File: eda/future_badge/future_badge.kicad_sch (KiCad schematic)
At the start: 0 parts

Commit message: schematic start
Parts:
- added D? (x4): LED_WS2812D_THT_5mm, 0_local:LED_D5.0mm-4_WS2812D_front, symbol 0_local:LED_WS2812D_THT_5mm
- added D? (x14): LED_THT_5mm, 0_local:LED_D5.0mm-2, symbol 0_local:LED_THT_5mm
- added U?: ESP-12F, RF_Module:ESP-12E, symbol RF_Module:ESP-12F
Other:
- note added: "battery choice, 3aaa?"
- note added: "capacitors"
- note added: "test pins for flashing mcu"
- note added: "usb choice? yes/no/flash only"
- note added: "voltage reg transistor"

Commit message: more stuff
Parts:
- removed D? (x8): LED_THT_5mm, 0_local:LED_D5.0mm-2, symbol 0_local:LED_THT_5mm
- removed U?: ESP-12F, RF_Module:ESP-12E, symbol RF_Module:ESP-12F
- added D? (x4): LED_Two_Color_CC_THT_3mm, 0_local:LED_D3.0mm-3-TwoColor_backsilk, symbol 0_local:LED_Two_Color_CC_THT_3mm
- added U?: ESP32-WROOM-32, RF_Module:ESP32-WROOM-32, symbol 0_local:ESP32-WROOM-32
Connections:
- new net: U?.1 (GND), U?.15 (GND), U?.38 (GND), U?.39 (GND)
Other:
- note removed: "test pins for flashing mcu"
- note removed: "usb choice? yes/no/flash only"
- note removed: "voltage reg transistor"
- moved on the sheet: D?

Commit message: more test code and esp32 sch and fp and 3d
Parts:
- removed D? (x6): LED_THT_5mm, 0_local:LED_D5.0mm-2, symbol 0_local:LED_THT_5mm
- removed U?: ESP32-WROOM-32, RF_Module:ESP32-WROOM-32, symbol 0_local:ESP32-WROOM-32
- added U?: ESP32-WROOM-32-DEVKIT, 0_local:ESP32_DEVKIT_V1, symbol 0_local:ESP32-WROOM-32-DEVKIT
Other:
- note removed: "battery choice, 3aaa?"
- note removed: "capacitors"
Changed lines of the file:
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@@
     (company "Crafted by @alt_bier a.k.a. Richard Gowen")
-  )
-  (text "battery choice, 3aaa?" (at 41.91 153.67 0)
-    (effects (font (size 1.27 1.27)) (justify left bottom))
-  )
-  (text "capacitors" (at 57.15 25.4 0)
-    (effects (font (size 1.27 1.27)) (justify left bottom))
   )
   (symbol (lib_id "0_local:LED_Two_Color_CC_THT_3mm") (at 64.77 120.65 0) (unit 1)
@@
     (pin "4")
   )
-  (symbol (lib_id "0_local:LED_THT_5mm") (at 128.27 121.92 0) (unit 1)
+  (symbol (lib_id "0_local:LED_Two_Color_CC_THT_3mm") (at 60.96 95.25 0) (unit 1)
     (in_bom yes) (on_board yes) (fields_autoplaced)
-    (property "Reference" "D?" (id 0) (at 126.6698 116.9756 0))
-    (property "Value" "LED_THT_5mm" (id 1) (at 126.6698 119.5125 0))
-    (property "Footprint" "0_local:LED_D5.0mm-2" (id 2) (at 128.27 128.27 0)
+    (property "Reference" "D?" (id 0) (at 59.7535 82.6602 0))
+    (property "Value" "LED_Two_Color_CC_THT_3mm" (id 1) (at 59.7535 85.1971 0))
+    (property "Footprint" "0_local:LED_D3.0mm-3-TwoColor_backsilk" (id 2) (at 62.23 107.95 0)
       (effects (font (size 1.27 1.27)) hide)
     )
-    (property "Datasheet" "~" (id 3) (at 128.27 121.92 0)
+    (property "Datasheet" "~" (id 3) (at 59.309 95.123 0)
       (effects (font (size 1.27 1.27)) hide)
     )
     (pin "1")
     (pin "2")
+    (pin "3")
   )
-  (symbol (lib_id "0_local:LED_THT_5mm") (at 124.46 107.95 0) (unit 1)
+  (symbol (lib_id "0_local:ESP32-WROOM-32-DEVKIT") (at 205.74 62.23 0) (unit 1)
     (in_bom yes) (on_board yes) (fields_autoplaced)
-    (property "Reference" "D?" (id 0) (at 122.8598 103.0056 0))
-    (property "Value" "LED_THT_5mm" (id 1) (at 122.8598 105.5425 0))
-    (property "Footprint" "0_local:LED_D5.0mm-2" (id 2) (at 124.46 114.3 0)
+    (property "Reference" "U?" (id 0) (at 205.74 21.7002 0))
+    (property "Value" "ESP32-WROOM-32-DEVKIT" (id 1) (at 205.74 24.2371 0))
+    (property "Footprint" "0_local:ESP32_DEVKIT_V1" (id 2) (at 206.121 100.965 0)
       (effects (font (size 1.27 1.27)) hide)
     )
-    (property "Datasheet" "~" (id 3) (at 124.46 107.95 0)
-      (effects (font (size 1.27 1.27)) hide)
-    )
-    (pin "1")
-    (pin "2")
-  )
-  (symbol (lib_id "0_local:LED_THT_5mm") (at 132.08 77.47 0) (unit 1)
-    (in_bom yes) (on_board yes) (fields_autoplaced)
-    (property "Reference" "D?" (id 0) (at 130.4798 72.5256 0))
-    (property "Value" "LED_THT_5mm" (id 1) (at 130.4798 75.0625 0))
-    (property "Footprint" "0_local:LED_D5.0mm-2" (id 2) (at 132.08 83.82 0)
-      (effects (font (size 1.27 1.27)) hide)
-    )
-    (property "Datasheet" "~" (id 3) (at 132.08 77.47 0)
-      (effects (font (size 1.27 1.27)) hide)
-    )
-    (pin "1")
-    (pin "2")
-  )
-  (symbol (lib_id "0_local:ESP32-WROOM-32") (at 201.93 62.23 0) (unit 1)
-    (in_bom yes) (on_board yes) (fields_autoplaced)
-    (property "Reference" "U?" (id 0) (at 203.9494 25.5102 0)
-      (effects (font (size 1.27 1.27)) (justify left))
-    )
-    (property "Value" "ESP32-WROOM-32" (id 1) (at 203.9494 28.0471 0)
-      (effects (font (size 1.27 1.27)) (justify left))
-    )
-    (property "Footprint" "RF_Module:ESP32-WROOM-32" (id 2) (at 201.93 100.33 0)
-      (effects (font (size 1.27 1.27)) hide)
-    )
-    (property "Datasheet" "https://www.espressif.com/sites/default/files/documentation/esp32-wroom-32_datasheet_en.pdf" (id 3) (at 194.31 60.96 0)
+    (property "Datasheet" "https://www.espressif.com/sites/default/files/documentation/esp32-wroom-32_datasheet_en.pdf" (id 3) (at 206.121 104.14 0)
       (effects (font (size 1.27 1.27)) hide)
     )
@@
     (pin "3")
     (pin "30")
-    (pin "31")
-    (pin "32")
-    (pin "33")
-    (pin "34")
-    (pin "35")
-    (pin "36")
-    (pin "37")
-    (pin "38")
-    (pin "39")
     (pin "4")
     (pin "5")
@@
     (pin "8")
     (pin "9")
-  )
-  (symbol (lib_id "0_local:LED_Two_Color_CC_THT_3mm") (at 60.96 95.25 0) (unit 1)
-    (in_bom yes) (on_board yes) (fields_autoplaced)
-    (property "Reference" "D?" (id 0) (at 59.7535 82.6602 0))
-    (property "Value" "LED_Two_Color_CC_THT_3mm" (id 1) (at 59.7535 85.1971 0))
-    (property "Footprint" "0_local:LED_D3.0mm-3-TwoColor_backsilk" (id 2) (at 62.23 107.95 0)
-      (effects (font (size 1.27 1.27)) hide)
-    )
-    (property "Datasheet" "~" (id 3) (at 59.309 95.123 0)
-      (effects (font (size 1.27 1.27)) hide)
-    )
-    (pin "1")
-    (pin "2")
-    (pin "3")
-  )
-  (symbol (lib_id "0_local:LED_THT_5mm") (at 116.84 77.47 0) (unit 1)
-    (in_bom yes) (on_board yes) (fields_autoplaced)
-    (property "Reference" "D?" (id 0) (at 115.2398 72.5256 0))
-    (property "Value" "LED_THT_5mm" (id 1) (at 115.2398 75.0625 0))
-    (property "Footprint" "0_local:LED_D5.0mm-2" (id 2) (at 116.84 83.82 0)
-      (effects (font (size 1.27 1.27)) hide)
-    )
-    (property "Datasheet" "~" (id 3) (at 116.84 77.47 0)
-      (effects (font (size 1.27 1.27)) hide)
-    )
-    (pin "1")
-    (pin "2")
-  )
-  (symbol (lib_id "0_local:LED_THT_5mm") (at 135.89 91.44 0) (unit 1)
-    (in_bom yes) (on_board yes) (fields_autoplaced)
-    (property "Reference" "D?" (id 0) (at 134.2898 86.4956 0))
-    (property "Value" "LED_THT_5mm" (id 1) (at 134.2898 89.0325 0))
-    (property "Footprint" "0_local:LED_D5.0mm-2" (id 2) (at 135.89 97.79 0)
-      (effects (font (size 1.27 1.27)) hide)
-    )
-    (property "Datasheet" "~" (id 3) (at 135.89 91.44 0)
-      (effects (font (size 1.27 1.27)) hide)
-    )
-    (pin "1")
-    (pin "2")
   )
   (symbol (lib_id "0_local:LED_Two_Color_CC_THT_3mm") (at 33.02 95.25 0) (unit 1)
@@
     (pin "2")
     (pin "3")
-  )
-  (symbol (lib_id "0_local:LED_THT_5mm") (at 116.84 90.17 0) (unit 1)
-    (in_bom yes) (on_board yes) (fields_autoplaced)
-    (property "Reference" "D?" (id 0) (at 115.2398 85.2256 0))
-    (property "Value" "LED_THT_5mm" (id 1) (at 115.2398 87.7625 0))
-    (property "Footprint" "0_local:LED_D5.0mm-2" (id 2) (at 116.84 96.52 0)
-      (effects (font (size 1.27 1.27)) hide)
-    )
-    (property "Datasheet" "~" (id 3) (at 116.84 90.17 0)
-      (effects (font (size 1.27 1.27)) hide)
-    )
-    (pin "1")
-    (pin "2")
   )
   (symbol (lib_id "0_local:LED_WS2812D_THT_5mm") (at 110.49 30.48 0) (unit 1)
@@
       (reference "D?") (unit 1) (value "LED_WS2812D_THT_5mm") (footprint "0_local:LED_D5.0mm-4_WS2812D_front")
     )
-    (path "/a037d820-7451-4555-a74a-d5b46dc9b440"
-      (reference "D?") (unit 1) (value "LED_THT_5mm") (footprint "0_local:LED_D5.0mm-2")
-    )
-    (path "/a04f141c-adb6-45fb-8bf8-24379808d0c2"
-      (reference "D?") (unit 1) (value "LED_THT_5mm") (footprint "0_local:LED_D5.0mm-2")
-    )
-    (path "/a35efc5a-3467-4fce-927e-110c01846fe8"
-      (reference "D?") (unit 1) (value "LED_THT_5mm") (footprint "0_local:LED_D5.0mm-2")
-    )
     (path "/bbd6d3b4-da4c-4698-baf3-c9cf2c3d909a"
       (reference "D?") (unit 1) (value "LED_Two_Color_CC_THT_3mm") (footprint "0_local:LED_D3.0mm-3-TwoColor_backsilk")
-    )
-    (path "/c33e8ea4-ac2d-4687-b4fc-69e62a70f84a"
-      (reference "D?") (unit 1) (value "LED_THT_5mm") (footprint "0_local:LED_D5.0mm-2")
-    )
-    (path "/c4ac28bf-6e28-42a5-a19a-1eace0b9bb29"
-      (reference "D?") (unit 1) (value "LED_THT_5mm") (footprint "0_local:LED_D5.0mm-2")
     )
     (path "/df140d56-8bce-499b-90a0-feb6d8703fe7"
       (reference "D?") (unit 1) (value "LED_Two_Color_CC_THT_3mm") (footprint "0_local:LED_D3.0mm-3-TwoColor_backsilk")
     )
-    (path "/e4b0e406-4667-41c0-a2f7-b60025f1da0c"
-      (reference "D?") (unit 1) (value "LED_THT_5mm") (footprint "0_local:LED_D5.0mm-2")
-    )
     (path "/f42b6bf3-1c1d-4df1-91d6-ff1e3bcd963b"
       (reference "D?") (unit 1) (value "LED_WS2812D_THT_5mm") (footprint "0_local:LED_D5.0mm-4_WS2812D_front")
     )
-    (path "/a6b69720-cdfd-468b-9c92-960dea5fc7b2"
-      (reference "U?") (unit 1) (value "ESP32-WROOM-32") (footprint "RF_Module:ESP32-WROOM-32")
+    (path "/bf6493ed-db90-49dc-bd81-929e56c37c92"
+      (reference "U?") (unit 1) (value "ESP32-WROOM-32-DEVKIT") (footprint "0_local:ESP32_DEVKIT_V1")
     )
   )

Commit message: updated schematic
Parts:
- removed D? (x3): LED_Two_Color_CC_THT_3mm, 0_local:LED_D3.0mm-3-TwoColor_backsilk, symbol 0_local:LED_Two_Color_CC_THT_3mm
- removed D? (x3): LED_WS2812D_THT_5mm, 0_local:LED_D5.0mm-4_WS2812D_front, symbol 0_local:LED_WS2812D_THT_5mm
- removed U?: ESP32-WROOM-32-DEVKIT, 0_local:ESP32_DEVKIT_V1, symbol 0_local:ESP32-WROOM-32-DEVKIT
- added C11, C12, C21, C22: 100nF, 0_local:C_Disc_D3.0mm_W2.0mm_P2.50mm_backsilk, symbol 0_local:C_Disc_D3
- added D12, D21, D22: LED_WS2812D_THT_5mm, 0_local:LED_D5.0mm-4_WS2812D_front, symbol 0_local:LED_WS2812D_THT_5mm
- added U1: ESP32-WROOM-32-DEVKIT, 0_local:ESP32_DEVKIT_V1, symbol 0_local:ESP32-WROOM-32-DEVKIT
- gave numbers to parts that had none: 2
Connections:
- net LED31: now reaches D1.1 (RA)
- net LED31: now also U1.27 (GPIO12)
- net GND: now reaches D1.2 (K)
- net GND: now also D11.3 (GND), C11.2, C12.2, C21.2, C22.2, D12.3 (GND), D21.3 (GND), D22.3 (GND), U1.2 (GND)
- net LED32: now reaches D1.3 (BA)
- net LED32: now also U1.28 (GPIO13)
- net NEO1-1: now reaches D11.1 (DOUT)
- net NEO1-1: now also D12.4 (DIN)
- net +3.3V: now reaches D11.2 (VDD)
- net +3.3V: now also C11.1, C12.1, C21.1, C22.1, D12.2 (VDD), D21.2 (VDD), D22.2 (VDD), U1.1 (3V3)
- net NEO1: now reaches D11.4 (DIN)
- net NEO1: now also U1.9 (GPIO18)
- new net NEO2: D21.4 (DIN), U1.10 (GPIO19)
- new net NEO2-1: D21.1 (DOUT), D22.4 (DIN)
- new net TCH1: U1.21 (GPIO32)
- no-connect marks 0 -> 2
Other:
- moved on the sheet: D1, D11

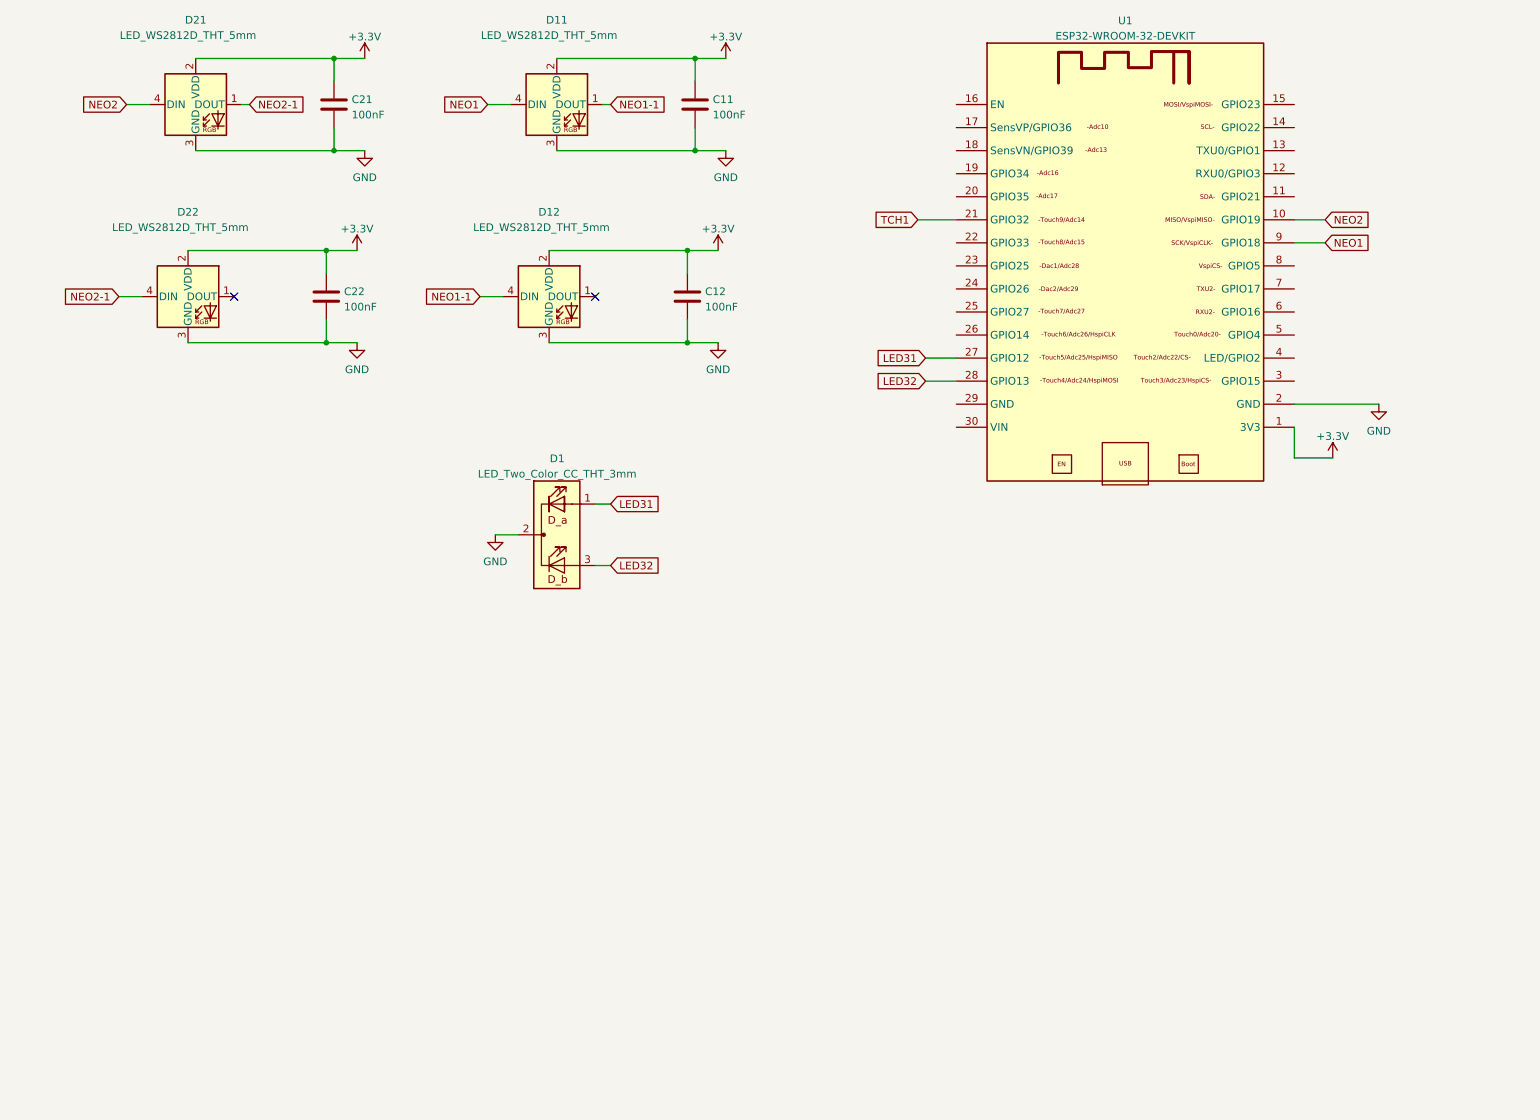
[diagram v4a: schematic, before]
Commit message: schematic and code and art updates
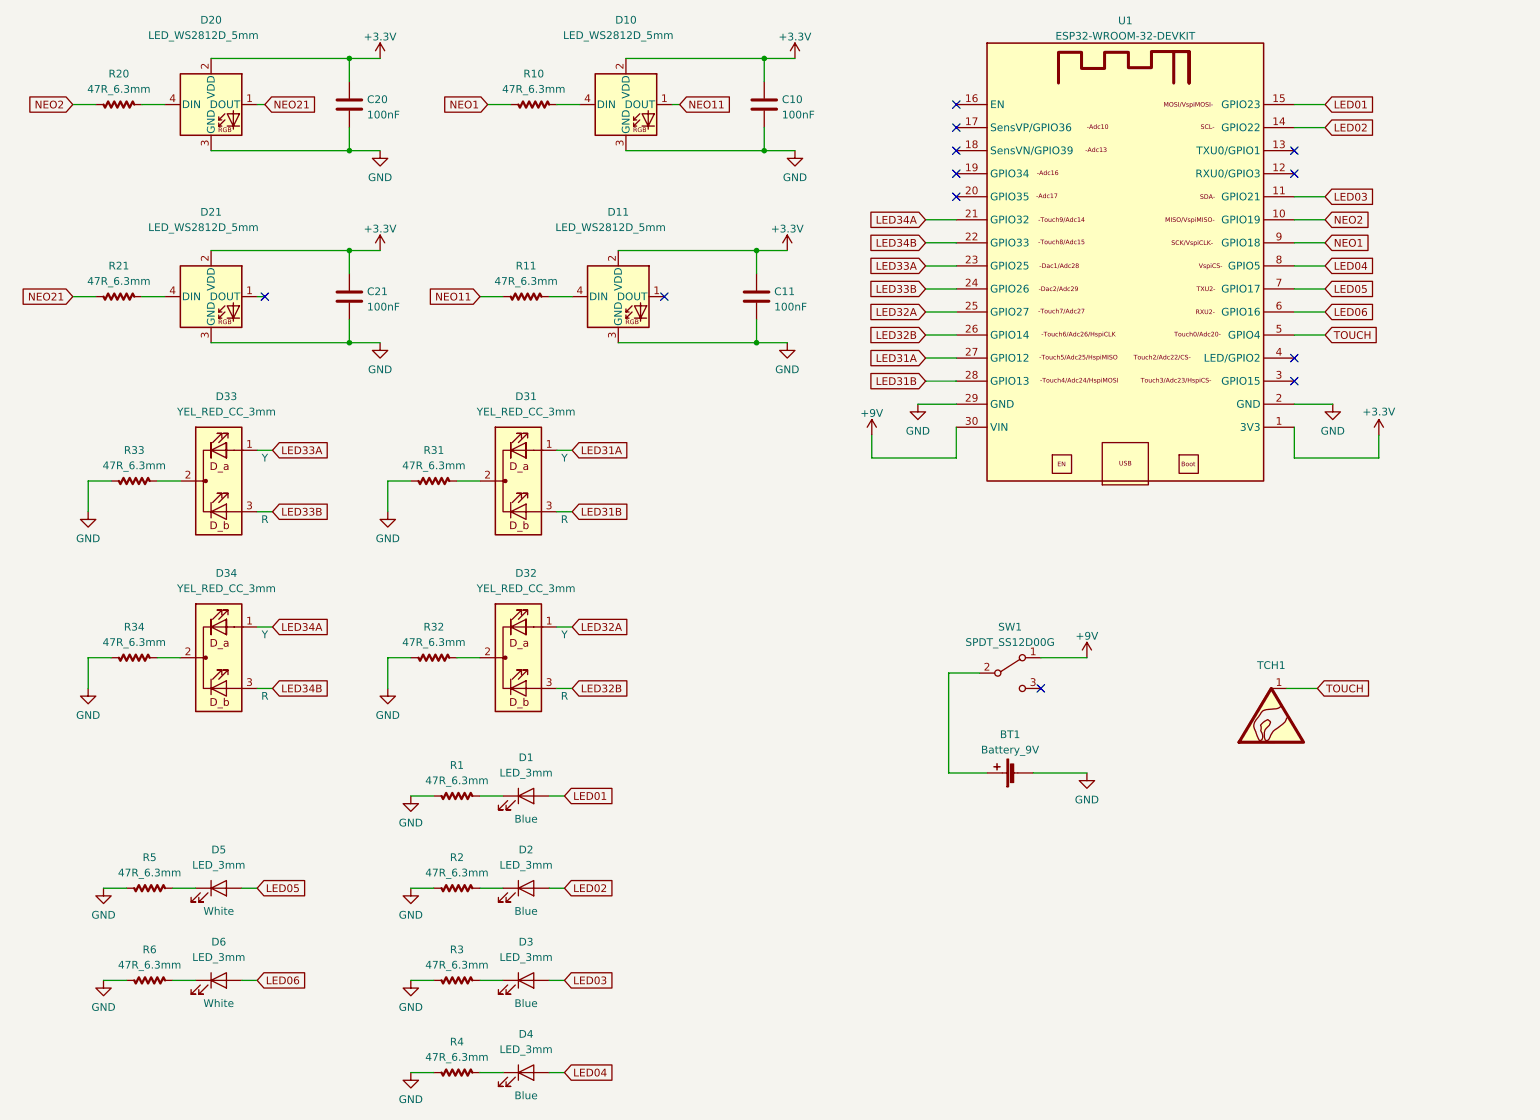
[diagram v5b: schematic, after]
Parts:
- removed C22: 100nF, 0_local:C_Disc_D3.0mm_W2.0mm_P2.50mm_backsilk, symbol 0_local:C_Disc_D3
- removed D22: LED_WS2812D_THT_5mm, 0_local:LED_D5.0mm-4_WS2812D_front, symbol 0_local:LED_WS2812D_THT_5mm
- added BT1: Battery_9V, 0_local:Battery_Lead_Wire_Connector, symbol 0_local:Battery_9V
- added C21: 100nF, 0_local:C_Disc_D3.0mm_W2.0mm_P2.50mm, symbol 0_local:C_Disc_D3
- added D1, D2, D3, D4, D5, D6: LED_3mm, 0_local:LED_D3.0mm-2, symbol 0_local:LED_THT_3mm
- added D21: LED_WS2812D_5mm, 0_local:LED_D5.0mm-4_WS2812D_front_new, symbol 0_local:LED_WS2812D_THT_5mm
- added D32, D33, D34: YEL_RED_CC_3mm, 0_local:LED_D3.0mm-3-TwoColor, symbol 0_local:LED_Two_Color_CC_THT_3mm
- added R1, R10, R11, R2, R20, R21, R3, R31, R32, R33, R34, R4, R5, R6: 47R_6.3mm, 0_local:R_Axial_DIN0207_L6.3mm_D2.5mm_P7.62mm_Horizontal, symbol 0_local:R_Axial_Z_L6.3
- added SW1: SPDT_SS12D00G, 0_local:SW_SPDT_Slide_SS12D00G-1P2T_3pin, symbol 0_local:SW_SPDT_SS12D00G
- added TCH1: SYM_Touch_lg, symbol 0_local:SYM_Touch_lg
- C10: renamed from C11; footprint 0_local:C_Disc_D3.0mm_W2.0mm_P2.50mm_backsilk -> 0_local:C_Disc_D3.0mm_W2.0mm_P2.50mm
- C11: renamed from C12; footprint 0_local:C_Disc_D3.0mm_W2.0mm_P2.50mm_backsilk -> 0_local:C_Disc_D3.0mm_W2.0mm_P2.50mm
- C20: renamed from C21; footprint 0_local:C_Disc_D3.0mm_W2.0mm_P2.50mm_backsilk -> 0_local:C_Disc_D3.0mm_W2.0mm_P2.50mm
- D10: renamed from D11; value LED_WS2812D_THT_5mm -> LED_WS2812D_5mm; footprint 0_local:LED_D5.0mm-4_WS2812D_front -> 0_local:LED_D5.0mm-4_WS2812D_front_new
- D11: renamed from D12; value LED_WS2812D_THT_5mm -> LED_WS2812D_5mm; footprint 0_local:LED_D5.0mm-4_WS2812D_front -> 0_local:LED_D5.0mm-4_WS2812D_front_new
- D20: renamed from D21; value LED_WS2812D_THT_5mm -> LED_WS2812D_5mm; footprint 0_local:LED_D5.0mm-4_WS2812D_front -> 0_local:LED_D5.0mm-4_WS2812D_front_new
- D31: renamed from D1; value LED_Two_Color_CC_THT_3mm -> YEL_RED_CC_3mm; footprint 0_local:LED_D3.0mm-3-TwoColor_backsilk -> 0_local:LED_D3.0mm-3-TwoColor; ColA (none) -> Y; ColB (none) -> R
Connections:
- net +3.3V: now also C21.1, D21.2 (VDD)
- net GND: now also U1.29 (GND), BT1.2 (-), C21.2, D21.3 (GND), R1.1, R2.1, R3.1, R31.1, R32.1, R33.1, R34.1, R4.1, R5.1, R6.1; no longer D31.2 (K)
- net NEO1: now also R10.1; no longer D10.4 (DIN)
- net NEO2: now also R20.1; no longer D20.4 (DIN)
- net LED03: now reaches U1.11 (GPIO21)
- net LED03: now also D3.2 (A)
- net LED02: now reaches U1.14 (GPIO22)
- net LED02: now also D2.2 (A)
- net LED01: now reaches U1.15 (GPIO23)
- net LED01: now also D1.2 (A)
- net LED34B: now reaches U1.22 (GPIO33)
- net LED34B: now also D34.3 (BA)
- net LED33A: now reaches U1.23 (GPIO25)
- net LED33A: now also D33.1 (RA)
- net LED33B: now reaches U1.24 (GPIO26)
- net LED33B: now also D33.3 (BA)
- net LED32A: now reaches U1.25 (GPIO27)
- net LED32A: now also D32.1 (RA)
- net LED32B: now reaches U1.26 (GPIO14)
- net LED32B: now also D32.3 (BA)
- net +9V: now reaches U1.30 (VIN)
- net +9V: now also SW1.1 (A)
- net TOUCH: now reaches U1.5 (GPIO4)
- net TOUCH: now also TCH1.1
- net LED06: now reaches U1.6 (GPIO16)
- net LED06: now also D6.2 (A)
- net LED05: now reaches U1.7 (GPIO17)
- net LED05: now also D5.2 (A)
- net LED04: now reaches U1.8 (GPIO5)
- net LED04: now also D4.2 (A)
- net LED31 renamed LED31A
- net LED32 renamed LED31B
- net NEO1-1: no longer names the net of D11.4 (DIN)
- net NEO1-1: now also R11.2; no longer D10.1 (DOUT)
- net NEO2-1 renamed NEO21
- net NEO21: now also R21.1
- net TCH1 renamed LED34A
- net LED34A: now also D34.1 (RA)
- new net: D32.2 (K), R32.2
- new net: D4.1 (K), R4.2
- new net: D31.2 (K), R31.2
- new net: D3.1 (K), R3.2
- new net: BT1.1 (+), SW1.2 (B)
- new net: D5.1 (K), R5.2
- new net: D33.2 (K), R33.2
- new net: D34.2 (K), R34.2
- new net: D20.4 (DIN), R20.2
- new net: D6.1 (K), R6.2
- new net: D10.4 (DIN), R10.2
- new net: D2.1 (K), R2.2
- new net: D1.1 (K), R1.2
- new net: D21.4 (DIN), R21.2
- new net NEO11: D10.1 (DOUT), R11.1
- no-connect marks 2 -> 12
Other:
- moved on the sheet: C10, C11, C20, D10, D11, D20, D31
